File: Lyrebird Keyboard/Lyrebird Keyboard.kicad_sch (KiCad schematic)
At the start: 95 parts, among them IC1 L7915CV, IC2 L78S15CV, IC3 MCP6022-E_SN, IC4 IR2113SPBF, IC5 IR2113SPBF, IC6 LM358DT, IC7 L7805ACD2T-TR, J1 WAV/ENV 4, J10 1776119-2, J11 1776119-2, J12 1776119-2, J13 MC-254-16-00-ST-DIP, J14 MC-254-16-00-ST-DIP, J15 MC-254-16-00-ST-DIP, J16 MC-254-16-00-ST-DIP, J17 MC-254-16-00-ST-DIP, J18 MC-254-16-00-ST-DIP, J19 MC-254-16-00-ST-DIP, J2 WAV/ENV 3, J20 1776119-2, J21 1776119-2, J3 WAV/ENV 2, J4 WAV/ENV 1, J5 TONE SRC 4, J6 TONE SRC 3, J7 TONE SRC 2, J8 TONE SRC 1, J9 1776119-2, Q1 BC848, Q2 BC848, Q3 IRFR2905ZTRPBF, Q4 IRFR2905ZTRPBF, Q5 IRFR2905ZTRPBF, Q6 IRFR2905ZTRPBF, U1 DF06S

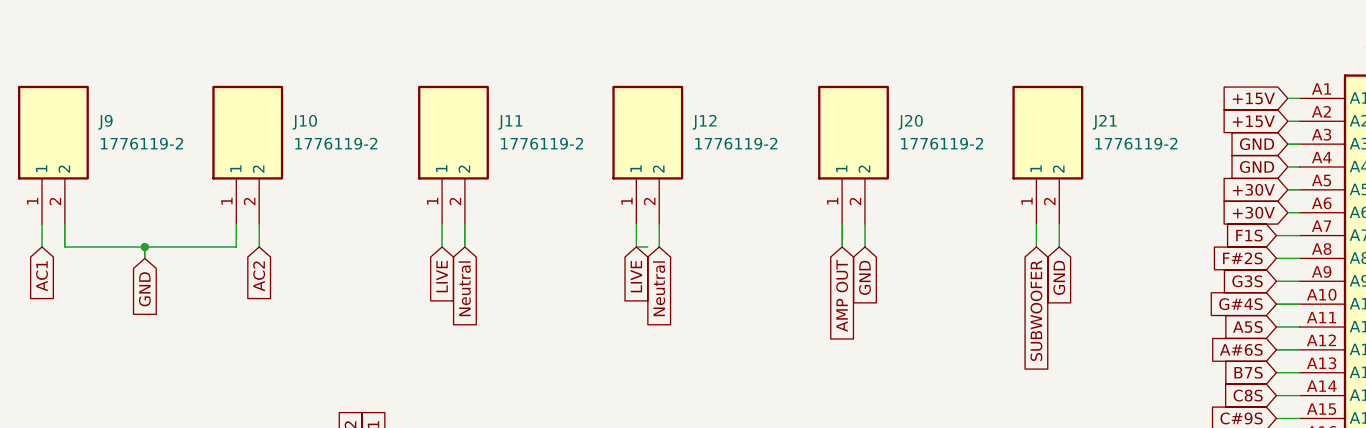
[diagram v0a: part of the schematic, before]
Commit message: additional tracks laid
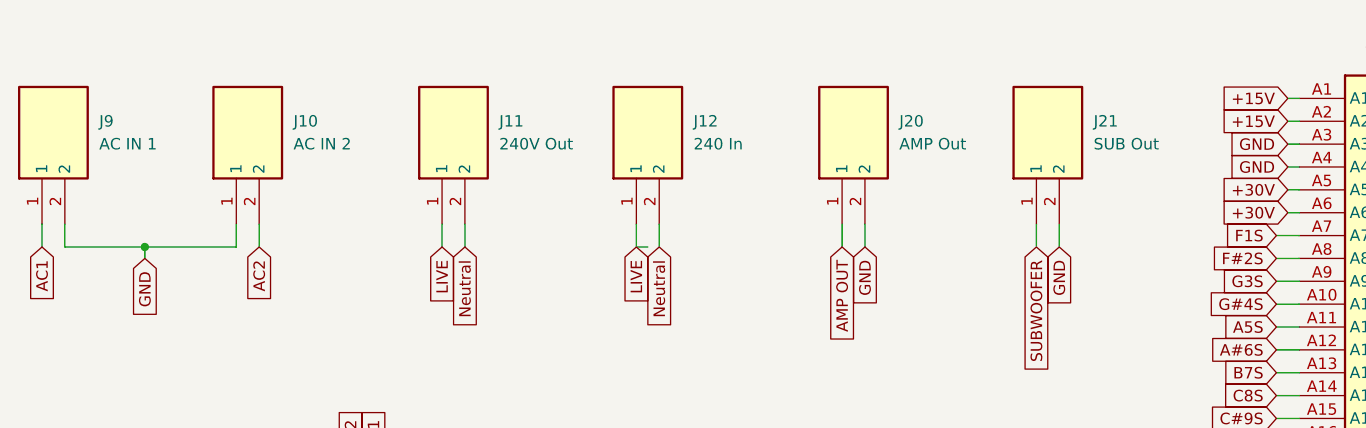
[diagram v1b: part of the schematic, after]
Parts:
- J10: value 1776119-2 -> AC IN 2
- J11: value 1776119-2 -> 240V Out
- J12: value 1776119-2 -> 240 In
- J20: value 1776119-2 -> AMP Out
- J21: value 1776119-2 -> SUB Out
- J9: value 1776119-2 -> AC IN 1
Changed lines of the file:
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@@
       (effects (font (size 1.27 1.27)) (justify right))
     )
-    (property "Value" "1776119-2" (at 144.78 39.37 90)
+    (property "Value" "SUB Out" (at 144.78 39.37 90)
       (effects (font (size 1.27 1.27)) (justify right))
     )
@@
       (effects (font (size 1.27 1.27)) (justify right))
     )
-    (property "Value" "1776119-2" (at 78.74 39.37 90)
+    (property "Value" "240V Out" (at 78.74 39.37 90)
       (effects (font (size 1.27 1.27)) (justify right))
     )
@@
       (effects (font (size 1.27 1.27)) (justify right))
     )
-    (property "Value" "1776119-2" (at 123.19 39.37 90)
+    (property "Value" "AMP Out" (at 123.19 39.37 90)
       (effects (font (size 1.27 1.27)) (justify right))
     )
@@
       (effects (font (size 1.27 1.27)) (justify right))
     )
-    (property "Value" "1776119-2" (at 55.88 39.37 90)
+    (property "Value" "AC IN 2" (at 55.88 39.37 90)
       (effects (font (size 1.27 1.27)) (justify right))
     )
@@
       (effects (font (size 1.27 1.27)) (justify right))
     )
-    (property "Value" "1776119-2" (at 34.29 39.37 90)
+    (property "Value" "AC IN 1" (at 34.29 39.37 90)
       (effects (font (size 1.27 1.27)) (justify right))
     )
@@
       (effects (font (size 1.27 1.27)) (justify right))
     )
-    (property "Value" "1776119-2" (at 100.33 39.37 90)
-      (effects (font (size 1.27 1.27)) (justify right))
-    )
+    (property "Value" "240 In" (at 100.33 39.37 90)
+      (effects (font (size 1.27 1.27)) (justify right))
+    )

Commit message: Added schematic definitions
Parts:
- removed R1: 4R7 5W, AXIAL-0.3, symbol SparkFun-Resistors:RESISTORAXIAL-0.3
- added R1: SQMR54K7J, SQMR54K7J, symbol SamacSys_Parts:SQMR54K7J
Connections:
- net +15V: no longer IC6.8 (VCC+)
- net +30V: now also R1.1
- net +5V: now also IC6.8 (VCC+), IC7.3 (OUTPUT)
- net +VT: now also R1.2
- net -15V: no longer IC6.4 (VCC-)
- net GND: now also IC6.4 (VCC-)
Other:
- note added: "Class D Amp Triangle wave Oscillator"
- note added: "Class D Amplifier"
- note added: "Class D Audio Encoder"
- note added: "Module Slots"
- note added: "Piano Key Headers"
- note added: "Power Supply"
- moved on the sheet: C16, C18, C19, C20, C21, C22, C23, C24, C25, C27, C3, C43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

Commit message: Tracks almost finished
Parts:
- removed J19: MC-254-16-00-ST-DIP, SHDR16W64P254_2X8_2798X910X910P, symbol SamacSys_Parts:MC-254-16-00-ST-DIP
- added J19: Triangle Test, Connector_PinHeader_2.54mm:PinHeader_1x01_P2.54mm_Vertical, symbol Connector:Conn_01x01_Pin
- added J22: Square Test, Connector_PinHeader_2.54mm:PinHeader_1x01_P2.54mm_Vertical, symbol Connector:Conn_01x01_Pin
- added J23: Bias Test Point 2, Connector_PinHeader_2.54mm:PinHeader_1x01_P2.54mm_Vertical, symbol Connector:Conn_01x01_Pin
- added J24: Bias Test Point 1, Connector_PinHeader_2.54mm:PinHeader_1x01_P2.54mm_Vertical, symbol Connector:Conn_01x01_Pin
- C1, C2, C3, C4: footprint CAPPRD750W85D1600H3350 -> SamacSys_Parts:CAPPRD750W85D1600H3350
- C16, C18, C21, C22, C23, C24, C25, C27: footprint EEE0JA152UAP -> SamacSys_Parts:EEE0JA152UAP
- C5: footprint CAPPRD200W55D500H1250 -> SamacSys_Parts:CAPPRD200W55D500H1250
- C6, C7, C8: footprint CAPPRD150W47D425H800 -> SamacSys_Parts:CAPPRD150W47D425H800
- D1: footprint DIOAD1405W86L465D235 -> SamacSys_Parts:DIOAD1405W86L465D235
- D2, D3, D4, D5, D6, D7: footprint DIOM5127X229N -> SamacSys_Parts:DIOM5127X229N
- IC1: footprint TO270P460X1020X2008-3P -> SamacSys_Parts:TO270P460X1020X2008-3P
- IC2: footprint TO255P460X1020X2008-3P -> SamacSys_Parts:TO255P460X1020X2008-3P
- IC3, IC6: footprint SOIC127P600X175-8N -> SamacSys_Parts:SOIC127P600X175-8N
- IC4, IC5: footprint SOIC127P1032X265-16N -> SamacSys_Parts:SOIC127P1032X265-16N
- IC7: footprint D2PAK-STB35NF10T4 -> SamacSys_Parts:D2PAK-STB35NF10T4
- J1, J2, J3, J4: footprint 877159306 -> SamacSys_Parts:877159306
- J10, J11, J12, J20, J21, J9: footprint 17761192 -> SamacSys_Parts:17761192
- J13, J14, J15, J16, J17, J18: footprint SHDR16W64P254_2X8_2798X910X910P -> SamacSys_Parts:SHDR16W64P254_2X8_2798X910X910P
- J5, J6, J7, J8: footprint 1001878410212TLF -> SamacSys_Parts:1001878410212TLF
- L1, L2: footprint SRN8040220M -> SamacSys_Parts:SRN8040220M
- Q3, Q4, Q5, Q6: footprint IRFR2905ZTRPBF -> SamacSys_Parts:IRFR2905ZTRPBF
- R1: footprint SQMR54K7J -> SamacSys_Parts:SQMR54K7J
- R17: footprint CT9EW104 -> SamacSys_Parts:CT9EW104
- R2: footprint RESAD1650W60L650D250 -> SamacSys_Parts:RESAD1650W60L650D250
- U1: footprint SOT508P985X260-4N -> SamacSys_Parts:SOT508P985X260-4N
- VR1: footprint 3362P_1 -> SamacSys_Parts:3362P_1
- VR2, VR3, VR4: footprint T73YP103KT20 -> SamacSys_Parts:T73YP103KT20
- Z1, Z2: footprint PDZVTFTR47B -> SamacSys_Parts:PDZVTFTR47B
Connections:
- net +30V: no longer J1.A5, J1.A6, J13.4, J14.4, J15.4, J16.4, J17.4, J18.4, J2.A5, J2.A6, J3.A5, J3.A6, J4.A5, J4.A6, J5.A5, J5.A6, J6.A5, J6.A6, J7.A5, J7.A6, J8.A5, J8.A6
- net A#18: now also J14.6; no longer J14.11
- net A#30: now also J15.4; no longer J15.11
- net A#42: now also J16.14; no longer J16.11
- net A#54: now also J17.12; no longer J17.11
- net A#6: now also J13.8; no longer J13.11
- net A#66: now also J18.10; no longer J18.11
- net A17: now also J14.5; no longer J14.9
- net A29: now also J15.3; no longer J15.9
- net A41: now also J16.11; no longer J16.9
- net A5: now also J13.7; no longer J13.9
- net A65: now also J18.7; no longer J18.9
- net B19: now also J14.7; no longer J14.13
- net B31: now also J15.5; no longer J15.13
- net B55: now also J17.11; no longer J17.13
- net B67: now also J18.9; no longer J18.13
- net B7: now also J13.9; no longer J13.13
- net C#21: now also J14.9; no longer J14.16
- net C#33: now also J15.7; no longer J15.16
- net C#45: now also J16.15; no longer J16.16
- net C#57: now also J17.13; no longer J17.16
- net C#69: now also J18.11; no longer J18.16
- net C#9: now also J13.11; no longer J13.16
- net C20: now also J14.8; no longer J14.15
- net C32: now also J15.6; no longer J15.15
- net C44: now also J16.16; no longer J16.15
- net C56: now also J17.14; no longer J17.15
- net C68: now also J18.12; no longer J18.15
- net C8: now also J13.10; no longer J13.15
- net D#11: now also J13.13; no longer J13.12
- net D#23: now also J14.11; no longer J14.12
- net D#35: now also J16.5; no longer J15.12
- net D#47: now also J17.3; no longer J16.12
- net D#59: now also J17.15; no longer J17.12
- net D#71: now also J18.13; no longer J18.12
- net D10: now also J13.12; no longer J13.14
- net D22: now also J14.10; no longer J14.14
- net D34: now also J16.6; no longer J15.14
- net D46: now also J17.4; no longer J16.14
- net D58: now also J17.16; no longer J17.14
- net E12: now also J13.14; no longer J13.10
- net E24: now also J14.12; no longer J14.10
- net E36: now also J16.8; no longer J15.10
- net E48: now also J17.6; no longer J16.10
- net E60: now also J18.4; no longer J17.10
- net E72: now also J18.16; no longer J18.10
- net F#14: now also J13.16; no longer J14.3
- net F#2: now also J13.4; no longer J13.3
- net F#26: now also J14.14; no longer J15.3
- net F#38: now also J16.10; no longer J16.3
- net F#50: now also J17.8; no longer J17.3
- net F#62: now also J18.6; no longer J18.3
- net F1: now also J13.3; no longer J13.1
- net F13: now also J13.15; no longer J14.1
- net F25: now also J14.13; no longer J15.1
- net F37: now also J16.7; no longer J16.1
- net F49: now also J17.5; no longer J17.1
- net F61: now also J18.3; no longer J18.1
- net F73: now also J18.15
- net G#16: now also J14.4; no longer J14.7
- net G#28: now also J14.16; no longer J15.7
- net G#4: now also J13.6; no longer J13.7
- net G#40: now also J16.12; no longer J16.7
- net G#52: now also J17.10; no longer J17.7
- net G#64: now also J18.8; no longer J18.7
- net G15: now also J14.3; no longer J14.5
- net G27: now also J14.15; no longer J15.5
- net G39: now also J16.9; no longer J16.5
- net G51: now also J17.7; no longer J17.5
- net GND: now also J1.A5, J1.A6, J13.1, J14.1, J15.1, J16.1, J17.1, J18.1, J2.A5, J2.A6, J3.A5, J3.A6, J4.A5, J4.A6, J5.A5, J5.A6, J6.A5, J6.A6, J7.A5, J7.A6, J8.A5, J8.A6; no longer J13.6, J13.8, J14.6, J14.8, J15.6, J15.8, J16.6, J16.8, J17.6, J17.8, J18.6, J18.8
- net SQUARE: now also J22.1 (Pin_1)
- net TRI WAVE OUT: now also J19.1 (Pin_1)
- net at IC3.2 (VINA-), VR3.1 (CCW), VR4.2 (WIPER): now also J24.1 (Pin_1)
- net at C19.1, IC3.6 (VINB-), R12.1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: now also J23.1 (Pin_1)
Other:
- moved on the sheet: IC5, Q1, R17

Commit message: Mainboard Complete
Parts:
- added J25: Pedals, CTB05083, symbol SamacSys_Parts:CTB0508_3
- J1: value WAV/ENV 4 -> WAV/ENV 4 (MIDI)
- J13: value MC-254-16-00-ST-DIP -> Keys 1 to 14
- J14: value MC-254-16-00-ST-DIP -> Keys 15 to 28
- J15: value MC-254-16-00-ST-DIP -> Keys 29 to 33
- J16: value MC-254-16-00-ST-DIP -> Keys 34 to 45
- J17: value MC-254-16-00-ST-DIP -> Keys 46 to 59
- J18: value MC-254-16-00-ST-DIP -> Keys 60 to 73
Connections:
- net +30V: now also J1.A6
- net GND: now also J25.3; no longer J1.A6
- net SOFT: now also J25.1
- net SUSTAIN: now also J25.2
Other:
- moved on the sheet: C16, C18, C19, C20, C21, C22, C23, C24, C25, C27, C43, C44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

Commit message: Working on Tone Generator
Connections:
- net +15V: now also J1.B1, J2.B1, J3.B1, J4.B1, J5.B1, J6.B1, J7.B1, J8.B1; no longer J1.A2, J2.A2, J3.A2, J4.A2, J5.A2, J6.A2, J7.A2, J8.A2
- net +30V: no longer J1.A6
- net +VT: now also J1.A6, J2.A6, J3.A6, J4.A6, J5.A6, J6.A6, J7.A6, J8.A6; no longer J1.B5, J2.B5, J3.B5, J4.B5, J5.B5, J6.B5, J7.B5, J8.B5
- net -15V: now also J1.A2, J2.A2, J3.A2, J4.A2, J5.A2, J6.A2, J7.A2, J8.A2; no longer J1.B1, J2.B1, J3.B1, J4.B1, J5.B1, J6.B1, J7.B1, J8.B1
- net A#18S: now also J1.B17, J2.B17, J3.B17, J4.B17, J5.B17, J6.B17, J7.B17, J8.B17; no longer J1.A24, J2.A24, J3.A24, J4.A24, J5.A24, J6.A24, J7.A24, J8.A24
- net A#30S: now also J1.B16, J2.B16, J3.B16, J4.B16, J5.B16, J6.B16, J7.B16, J8.B16; no longer J1.A36, J2.A36, J3.A36, J4.A36, J5.A36, J6.A36, J7.A36, J8.A36
- net A#42S: now also J1.B15, J2.B15, J3.B15, J4.B15, J5.B15, J6.B15, J7.B15, J8.B15; no longer J1.A48, J2.A48, J3.A48, J4.A48, J5.A48, J6.A48, J7.A48, J8.A48
- net A#54S: now also J1.B14, J2.B14, J3.B14, J4.B14, J5.B14, J6.B14, J7.B14, J8.B14; no longer J1.B32, J2.B32, J3.B32, J4.B32, J5.B32, J6.B32, J7.B32, J8.B32
- net A#66S: now also J1.B13, J2.B13, J3.B13, J4.B13, J5.B13, J6.B13, J7.B13, J8.B13; no longer J1.B20, J2.B20, J3.B20, J4.B20, J5.B20, J6.B20, J7.B20, J8.B20
- net A#6S: now also J1.B18, J2.B18, J3.B18, J4.B18, J5.B18, J6.B18, J7.B18, J8.B18; no longer J1.A12, J2.A12, J3.A12, J4.A12, J5.A12, J6.A12, J7.A12, J8.A12
- net A17S: now also J1.A45, J2.A45, J3.A45, J4.A45, J5.A45, J6.A45, J7.A45, J8.A45; no longer J1.A23, J2.A23, J3.A23, J4.A23, J5.A23, J6.A23, J7.A23, J8.A23
- net A29S: now also J1.A46, J2.A46, J3.A46, J4.A46, J5.A46, J6.A46, J7.A46, J8.A46; no longer J1.A35, J2.A35, J3.A35, J4.A35, J5.A35, J6.A35, J7.A35, J8.A35
- net A53S: now also J1.A48, J2.A48, J3.A48, J4.A48, J5.A48, J6.A48, J7.A48, J8.A48; no longer J1.B33, J2.B33, J3.B33, J4.B33, J5.B33, J6.B33, J7.B33, J8.B33
- net A5S: now also J1.A44, J2.A44, J3.A44, J4.A44, J5.A44, J6.A44, J7.A44, J8.A44; no longer J1.A11, J2.A11, J3.A11, J4.A11, J5.A11, J6.A11, J7.A11, J8.A11
- net A65S: now also J1.A49, J2.A49, J3.A49, J4.A49, J5.A49, J6.A49, J7.A49, J8.A49; no longer J1.B21, J2.B21, J3.B21, J4.B21, J5.B21, J6.B21, J7.B21, J8.B21
- net B19S: now also J1.B23, J2.B23, J3.B23, J4.B23, J5.B23, J6.B23, J7.B23, J8.B23; no longer J1.A25, J2.A25, J3.A25, J4.A25, J5.A25, J6.A25, J7.A25, J8.A25
- net B31S: now also J1.B22, J2.B22, J3.B22, J4.B22, J5.B22, J6.B22, J7.B22, J8.B22; no longer J1.A37, J2.A37, J3.A37, J4.A37, J5.A37, J6.A37, J7.A37, J8.A37
- net B43S: now also J1.B21, J2.B21, J3.B21, J4.B21, J5.B21, J6.B21, J7.B21, J8.B21; no longer J1.A49, J2.A49, J3.A49, J4.A49, J5.A49, J6.A49, J7.A49, J8.A49
- net B55S: now also J1.B20, J2.B20, J3.B20, J4.B20, J5.B20, J6.B20, J7.B20, J8.B20; no longer J1.B31, J2.B31, J3.B31, J4.B31, J5.B31, J6.B31, J7.B31, J8.B31
- net B7S: now also J1.B24, J2.B24, J3.B24, J4.B24, J5.B24, J6.B24, J7.B24, J8.B24; no longer J1.A13, J2.A13, J3.A13, J4.A13, J5.A13, J6.A13, J7.A13, J8.A13
- net C#21S: now also J1.B35, J2.B35, J3.B35, J4.B35, J5.B35, J6.B35, J7.B35, J8.B35; no longer J1.A27, J2.A27, J3.A27, J4.A27, J5.A27, J6.A27, J7.A27, J8.A27
- net C#33S: now also J1.B34, J2.B34, J3.B34, J4.B34, J5.B34, J6.B34, J7.B34, J8.B34; no longer J1.A39, J2.A39, J3.A39, J4.A39, J5.A39, J6.A39, J7.A39, J8.A39
- net C#45S: now also J1.B33, J2.B33, J3.B33, J4.B33, J5.B33, J6.B33, J7.B33, J8.B33; no longer J1.B41, J2.B41, J3.B41, J4.B41, J5.B41, J6.B41, J7.B41, J8.B41
- net C#57S: now also J1.B32, J2.B32, J3.B32, J4.B32, J5.B32, J6.B32, J7.B32, J8.B32; no longer J1.B29, J2.B29, J3.B29, J4.B29, J5.B29, J6.B29, J7.B29, J8.B29
- net C#69S: now also J1.B31, J2.B31, J3.B31, J4.B31, J5.B31, J6.B31, J7.B31, J8.B31; no longer J1.B17, J2.B17, J3.B17, J4.B17, J5.B17, J6.B17, J7.B17, J8.B17
- net C#9S: now also J1.B36, J2.B36, J3.B36, J4.B36, J5.B36, J6.B36, J7.B36, J8.B36; no longer J1.A15, J2.A15, J3.A15, J4.A15, J5.A15, J6.A15, J7.A15, J8.A15
- net C20S: now also J1.B29, J2.B29, J3.B29, J4.B29, J5.B29, J6.B29, J7.B29, J8.B29; no longer J1.A26, J2.A26, J3.A26, J4.A26, J5.A26, J6.A26, J7.A26, J8.A26
- net C32S: now also J1.B28, J2.B28, J3.B28, J4.B28, J5.B28, J6.B28, J7.B28, J8.B28; no longer J1.A38, J2.A38, J3.A38, J4.A38, J5.A38, J6.A38, J7.A38, J8.A38
- net C44S: now also J1.B27, J2.B27, J3.B27, J4.B27, J5.B27, J6.B27, J7.B27, J8.B27; no longer J1.B42, J2.B42, J3.B42, J4.B42, J5.B42, J6.B42, J7.B42, J8.B42
- net C56S: now also J1.B26, J2.B26, J3.B26, J4.B26, J5.B26, J6.B26, J7.B26, J8.B26; no longer J1.B30, J2.B30, J3.B30, J4.B30, J5.B30, J6.B30, J7.B30, J8.B30
- net C68S: now also J1.B25, J2.B25, J3.B25, J4.B25, J5.B25, J6.B25, J7.B25, J8.B25; no longer J1.B18, J2.B18, J3.B18, J4.B18, J5.B18, J6.B18, J7.B18, J8.B18
- net C8S: now also J1.B30, J2.B30, J3.B30, J4.B30, J5.B30, J6.B30, J7.B30, J8.B30; no longer J1.A14, J2.A14, J3.A14, J4.A14, J5.A14, J6.A14, J7.A14, J8.A14
- net D#11S: now also J1.A38, J2.A38, J3.A38, J4.A38, J5.A38, J6.A38, J7.A38, J8.A38; no longer J1.A17, J2.A17, J3.A17, J4.A17, J5.A17, J6.A17, J7.A17, J8.A17
- net D#23S: now also J1.A39, J2.A39, J3.A39, J4.A39, J5.A39, J6.A39, J7.A39, J8.A39; no longer J1.A29, J2.A29, J3.A29, J4.A29, J5.A29, J6.A29, J7.A29, J8.A29
- net D#35S: now also J1.A40, J2.A40, J3.A40, J4.A40, J5.A40, J6.A40, J7.A40, J8.A40; no longer J1.A41, J2.A41, J3.A41, J4.A41, J5.A41, J6.A41, J7.A41, J8.A41
- net D#47S: now also J1.A41, J2.A41, J3.A41, J4.A41, J5.A41, J6.A41, J7.A41, J8.A41; no longer J1.B39, J2.B39, J3.B39, J4.B39, J5.B39, J6.B39, J7.B39, J8.B39
- net D#59S: now also J1.A42, J2.A42, J3.A42, J4.A42, J5.A42, J6.A42, J7.A42, J8.A42; no longer J1.B27, J2.B27, J3.B27, J4.B27, J5.B27, J6.B27, J7.B27, J8.B27
- net D#71S: now also J1.A43, J2.A43, J3.A43, J4.A43, J5.A43, J6.A43, J7.A43, J8.A43; no longer J1.B15, J2.B15, J3.B15, J4.B15, J5.B15, J6.B15, J7.B15, J8.B15
- net D10S: now also J1.B42, J2.B42, J3.B42, J4.B42, J5.B42, J6.B42, J7.B42, J8.B42; no longer J1.A16, J2.A16, J3.A16, J4.A16, J5.A16, J6.A16, J7.A16, J8.A16
- net D22S: now also J1.B41, J2.B41, J3.B41, J4.B41, J5.B41, J6.B41, J7.B41, J8.B41; no longer J1.A28, J2.A28, J3.A28, J4.A28, J5.A28, J6.A28, J7.A28, J8.A28
- net D34S: now also J1.B40, J2.B40, J3.B40, J4.B40, J5.B40, J6.B40, J7.B40, J8.B40; no longer J1.A40, J2.A40, J3.A40, J4.A40, J5.A40, J6.A40, J7.A40, J8.A40
- net D46S: now also J1.B39, J2.B39, J3.B39, J4.B39, J5.B39, J6.B39, J7.B39, J8.B39; no longer J1.B40, J2.B40, J3.B40, J4.B40, J5.B40, J6.B40, J7.B40, J8.B40
- net D58S: now also J1.B38, J2.B38, J3.B38, J4.B38, J5.B38, J6.B38, J7.B38, J8.B38; no longer J1.B28, J2.B28, J3.B28, J4.B28, J5.B28, J6.B28, J7.B28, J8.B28
- net D70S: now also J1.B37, J2.B37, J3.B37, J4.B37, J5.B37, J6.B37, J7.B37, J8.B37; no longer J1.B16, J2.B16, J3.B16, J4.B16, J5.B16, J6.B16, J7.B16, J8.B16
- net E12S: now also J1.A32, J2.A32, J3.A32, J4.A32, J5.A32, J6.A32, J7.A32, J8.A32; no longer J1.A18, J2.A18, J3.A18, J4.A18, J5.A18, J6.A18, J7.A18, J8.A18
- net E24S: now also J1.A33, J2.A33, J3.A33, J4.A33, J5.A33, J6.A33, J7.A33, J8.A33; no longer J1.A30, J2.A30, J3.A30, J4.A30, J5.A30, J6.A30, J7.A30, J8.A30
- net E36S: now also J1.A34, J2.A34, J3.A34, J4.A34, J5.A34, J6.A34, J7.A34, J8.A34; no longer J1.A42, J2.A42, J3.A42, J4.A42, J5.A42, J6.A42, J7.A42, J8.A42
- net E48S: now also J1.A35, J2.A35, J3.A35, J4.A35, J5.A35, J6.A35, J7.A35, J8.A35; no longer J1.B38, J2.B38, J3.B38, J4.B38, J5.B38, J6.B38, J7.B38, J8.B38
- net E60S: now also J1.A36, J2.A36, J3.A36, J4.A36, J5.A36, J6.A36, J7.A36, J8.A36; no longer J1.B26, J2.B26, J3.B26, J4.B26, J5.B26, J6.B26, J7.B26, J8.B26
- net E72S: now also J1.A37, J2.A37, J3.A37, J4.A37, J5.A37, J6.A37, J7.A37, J8.A37; no longer J1.B14, J2.B14, J3.B14, J4.B14, J5.B14, J6.B14, J7.B14, J8.B14
- net F#26S: now also J1.A21, J2.A21, J3.A21, J4.A21, J5.A21, J6.A21, J7.A21, J8.A21; no longer J1.A32, J2.A32, J3.A32, J4.A32, J5.A32, J6.A32, J7.A32, J8.A32
- net F#2S: now also J1.A19, J2.A19, J3.A19, J4.A19, J5.A19, J6.A19, J7.A19, J8.A19; no longer J1.A8, J2.A8, J3.A8, J4.A8, J5.A8, J6.A8, J7.A8, J8.A8
- net F#38S: now also J1.A22, J2.A22, J3.A22, J4.A22, J5.A22, J6.A22, J7.A22, J8.A22; no longer J1.A44, J2.A44, J3.A44, J4.A44, J5.A44, J6.A44, J7.A44, J8.A44
- net F#50S: now also J1.A23, J2.A23, J3.A23, J4.A23, J5.A23, J6.A23, J7.A23, J8.A23; no longer J1.B36, J2.B36, J3.B36, J4.B36, J5.B36, J6.B36, J7.B36, J8.B36
- net F#62S: now also J1.A24, J2.A24, J3.A24, J4.A24, J5.A24, J6.A24, J7.A24, J8.A24; no longer J1.B24, J2.B24, J3.B24, J4.B24, J5.B24, J6.B24, J7.B24, J8.B24
- net F13S: now also J1.A26, J2.A26, J3.A26, J4.A26, J5.A26, J6.A26, J7.A26, J8.A26; no longer J1.A19, J2.A19, J3.A19, J4.A19, J5.A19, J6.A19, J7.A19, J8.A19
- net F1S: now also J1.A25, J2.A25, J3.A25, J4.A25, J5.A25, J6.A25, J7.A25, J8.A25; no longer J1.A7, J2.A7, J3.A7, J4.A7, J5.A7, J6.A7, J7.A7, J8.A7
- net F25S: now also J1.A27, J2.A27, J3.A27, J4.A27, J5.A27, J6.A27, J7.A27, J8.A27; no longer J1.A31, J2.A31, J3.A31, J4.A31, J5.A31, J6.A31, J7.A31, J8.A31
- net F37S: now also J1.A28, J2.A28, J3.A28, J4.A28, J5.A28, J6.A28, J7.A28, J8.A28; no longer J1.A43, J2.A43, J3.A43, J4.A43, J5.A43, J6.A43, J7.A43, J8.A43
- net F49S: now also J1.A29, J2.A29, J3.A29, J4.A29, J5.A29, J6.A29, J7.A29, J8.A29; no longer J1.B37, J2.B37, J3.B37, J4.B37, J5.B37, J6.B37, J7.B37, J8.B37
- net F61S: now also J1.A30, J2.A30, J3.A30, J4.A30, J5.A30, J6.A30, J7.A30, J8.A30; no longer J1.B25, J2.B25, J3.B25, J4.B25, J5.B25, J6.B25, J7.B25, J8.B25
- net F73S: now also J1.A31, J2.A31, J3.A31, J4.A31, J5.A31, J6.A31, J7.A31, J8.A31; no longer J1.B13, J2.B13, J3.B13, J4.B13, J5.B13, J6.B13, J7.B13, J8.B13
- net G#16S: now also J1.A8, J2.A8, J3.A8, J4.A8, J5.A8, J6.A8, J7.A8, J8.A8; no longer J1.A22, J2.A22, J3.A22, J4.A22, J5.A22, J6.A22, J7.A22, J8.A22
- net G#28S: now also J1.A9, J2.A9, J3.A9, J4.A9, J5.A9, J6.A9, J7.A9, J8.A9; no longer J1.A34, J2.A34, J3.A34, J4.A34, J5.A34, J6.A34, J7.A34, J8.A34
- net G#40S: now also J1.A10, J2.A10, J3.A10, J4.A10, J5.A10, J6.A10, J7.A10, J8.A10; no longer J1.A46, J2.A46, J3.A46, J4.A46, J5.A46, J6.A46, J7.A46, J8.A46
- net G#4S: now also J1.A7, J2.A7, J3.A7, J4.A7, J5.A7, J6.A7, J7.A7, J8.A7; no longer J1.A10, J2.A10, J3.A10, J4.A10, J5.A10, J6.A10, J7.A10, J8.A10
- net G#52S: now also J1.A11, J2.A11, J3.A11, J4.A11, J5.A11, J6.A11, J7.A11, J8.A11; no longer J1.B34, J2.B34, J3.B34, J4.B34, J5.B34, J6.B34, J7.B34, J8.B34
- net G#64S: now also J1.A12, J2.A12, J3.A12, J4.A12, J5.A12, J6.A12, J7.A12, J8.A12; no longer J1.B22, J2.B22, J3.B22, J4.B22, J5.B22, J6.B22, J7.B22, J8.B22
- net G15S: now also J1.A14, J2.A14, J3.A14, J4.A14, J5.A14, J6.A14, J7.A14, J8.A14; no longer J1.A21, J2.A21, J3.A21, J4.A21, J5.A21, J6.A21, J7.A21, J8.A21
- net G27S: now also J1.A15, J2.A15, J3.A15, J4.A15, J5.A15, J6.A15, J7.A15, J8.A15; no longer J1.A33, J2.A33, J3.A33, J4.A33, J5.A33, J6.A33, J7.A33, J8.A33
- net G39S: now also J1.A16, J2.A16, J3.A16, J4.A16, J5.A16, J6.A16, J7.A16, J8.A16; no longer J1.A45, J2.A45, J3.A45, J4.A45, J5.A45, J6.A45, J7.A45, J8.A45
- net G3S: now also J1.A13, J2.A13, J3.A13, J4.A13, J5.A13, J6.A13, J7.A13, J8.A13; no longer J1.A9, J2.A9, J3.A9, J4.A9, J5.A9, J6.A9, J7.A9, J8.A9
- net G51S: now also J1.A17, J2.A17, J3.A17, J4.A17, J5.A17, J6.A17, J7.A17, J8.A17; no longer J1.B35, J2.B35, J3.B35, J4.B35, J5.B35, J6.B35, J7.B35, J8.B35
- net G63S: now also J1.A18, J2.A18, J3.A18, J4.A18, J5.A18, J6.A18, J7.A18, J8.A18; no longer J1.B23, J2.B23, J3.B23, J4.B23, J5.B23, J6.B23, J7.B23, J8.B23
- net GND: now also J1.B5, J2.B5, J3.B5, J4.B5, J5.B5, J6.B5, J7.B5, J8.B5; no longer J2.A6, J3.A6, J4.A6, J5.A6, J6.A6, J7.A6, J8.A6
